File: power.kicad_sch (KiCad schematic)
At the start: 10 parts, among them SW1 SW_SPST, U2 LTC3440EMS

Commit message: Use proper footprints for custom symbols
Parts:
- SW1: footprint (none) -> Button_Switch_SMD:SW_DIP_SPSTx01_Slide_9.78x4.72mm_W8.61mm_P2.54mm
- U2: footprint SOP50P490X110-10N -> Local_Library:SOP50P490X110-10N
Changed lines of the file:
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@@
       (effects (font (size 1.27 1.27)) hide)
     )
-    (property "Footprint" "" (id 2) (at 107.95 87.63 0)
+    (property "Footprint" "Button_Switch_SMD:SW_DIP_SPSTx01_Slide_9.78x4.72mm_W8.61mm_P2.54mm" (id 2) (at 107.95 87.63 0)
       (effects (font (size 1.27 1.27)) hide)
     )
@@
     (property "Reference" "U2" (id 0) (at 139.7 81.28 0))
     (property "Value" "LTC3440EMS" (id 1) (at 151.13 99.06 0))
-    (property "Footprint" "SOP50P490X110-10N" (id 2) (at 151.13 95.25 0)
+    (property "Footprint" "Local_Library:SOP50P490X110-10N" (id 2) (at 151.13 95.25 0)
       (effects (font (size 1.27 1.27)) (justify bottom) hide)
     )

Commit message: Improve DCDC converter diagram
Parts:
- U2: footprint Local_Library:SOP50P490X110-10N -> Package_SO:MSOP-10_3x3mm_P0.5mm
- renumbered C9 to C8, C8 to C9, R6 to R5, R5 to R6
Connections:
- net GND: now also R6.1; no longer R6.2
- net at U2.1 (RT): now also R6.2; no longer R6.1
- net FB: no longer names the net of R3.2, R4.1, R5.1, U2.9 (FB)
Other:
- company: Authors: H. Fedarovich, I. Kajdan -> Authors: A. Kotkov, I. Kajdan
- moved on the sheet: C10, C8, C9, L1, R3, R4, R5, R6, SW1, U2

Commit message: Arrange footprints
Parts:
- C10, C8: symbol Device:C_Small -> Device:C_Polarized_Small
- SW1: footprint Button_Switch_SMD:SW_DIP_SPSTx01_Slide_9.78x4.72mm_W8.61mm_P2.54mm -> Button_Switch_THT:SW_Slide_1P2T_CK_OS102011MS2Q; symbol Switch:SW_SPST -> Switch:SW_SPDT
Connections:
- net +3.3V: now also C8.1; no longer C8.2
- net +BATT: now also SW1.2 (B); no longer SW1.1 (A)
- net GND: now also C8.2; no longer C8.1
- net at C10.1, U2.7 (VIN), U2.8 (~{SHDN}/SS): now also SW1.1 (A); no longer SW1.2 (B)
- no-connect marks 1 -> 2

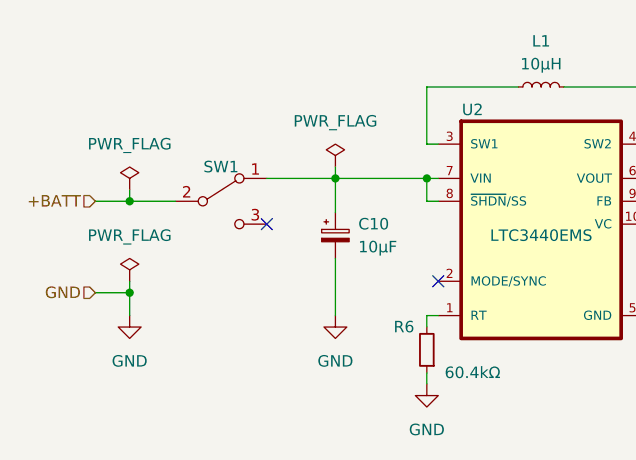
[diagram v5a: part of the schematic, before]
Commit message: Use more appropriate MCU pins for peripherals
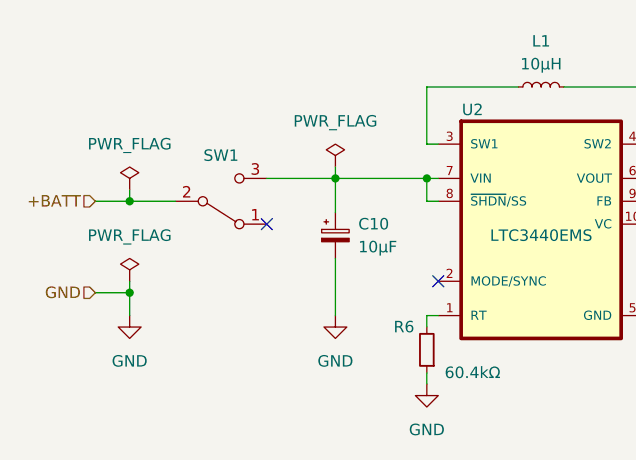
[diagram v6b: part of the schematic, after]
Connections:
- net at C10.1, U2.7 (VIN), U2.8 (~{SHDN}/SS): now also SW1.3 (C); no longer SW1.1 (A)
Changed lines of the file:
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@@
     (pin "2")
   )
-  (symbol (lib_id "Switch:SW_SPDT") (at 116.84 99.06 0) (unit 1)
+  (symbol (lib_id "Switch:SW_SPDT") (at 116.84 99.06 0) (mirror x) (unit 1)
     (in_bom yes) (on_board yes) (fields_autoplaced)
-    (property "Reference" "SW1" (id 0) (at 116.84 95.25 0))
-    (property "Value" "SW_SPST" (id 1) (at 116.84 95.25 0)
+    (property "Reference" "SW1" (id 0) (at 116.84 93.98 0))
+    (property "Value" "SW_SPST" (id 1) (at 116.84 102.87 0)
       (effects (font (size 1.27 1.27)) hide)
     )
